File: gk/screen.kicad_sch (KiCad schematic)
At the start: 8 parts, among them J3 Conn_02x27_Top_Bottom, U5 PT4110E89E

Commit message: Update pcb
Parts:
- added C78: 100n, Capacitor_SMD:C_0603_1608Metric, symbol Device:C
- added J9: Conn_01x06, Connector_FFC-FPC:TE_0-1734839-6_1x06-1MP_P0.5mm_Horizontal, symbol Connector_Generic:Conn_01x06
- added R56: 10k, Resistor_SMD:R_0603_1608Metric, symbol Device:R
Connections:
- net GND: now also C78.2, J9.6 (Pin_6), R56.2
- net VCC: now also C78.1, J9.3 (Pin_3)
- new net CTP_INT: J9.5 (Pin_5)
- new net CTP_NRESET: J9.4 (Pin_4), R56.1
- new net I2C4_SCL: J9.1 (Pin_1)
- new net I2C4_SDA: J9.2 (Pin_2)
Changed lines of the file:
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@@
   (junction (at 105.41 54.61) (diameter 0) (color 0 0 0 0)
   )
+  (junction (at 179.07 52.07) (diameter 0) (color 0 0 0 0)
+  )
   (junction (at 140.97 82.55) (diameter 0) (color 0 0 0 0)
   )
@@
   (junction (at 63.5 58.42) (diameter 0) (color 0 0 0 0)
   )
+  (junction (at 209.55 62.23) (diameter 0) (color 0 0 0 0)
+  )
   (junction (at 86.36 48.26) (diameter 0) (color 0 0 0 0)
   )
@@
   (junction (at 88.9 60.96) (diameter 0) (color 0 0 0 0)
   )
+  (junction (at 179.07 62.23) (diameter 0) (color 0 0 0 0)
+  )
   (junction (at 46.99 58.42) (diameter 0) (color 0 0 0 0)
+  )
+  (junction (at 209.55 54.61) (diameter 0) (color 0 0 0 0)
   )
   (no_connect (at 134.62 102.87))
@@
     (stroke (width 0) (type default))
   )
+  (wire (pts (xy 209.55 62.23) (xy 231.14 62.23))
+    (stroke (width 0) (type default))
+  )
   (wire (pts (xy 73.66 69.85) (xy 73.66 67.31))
     (stroke (width 0) (type default))
@@
     (stroke (width 0) (type default))
   )
+  (wire (pts (xy 217.17 54.61) (xy 217.17 57.15))
+    (stroke (width 0) (type default))
+  )
+  (wire (pts (xy 207.01 54.61) (xy 209.55 54.61))
+    (stroke (width 0) (type default))
+  )
   (wire (pts (xy 105.41 48.26) (xy 105.41 54.61))
     (stroke (width 0) (type default))
@@
     (stroke (width 0) (type default))
   )
+  (wire (pts (xy 179.07 62.23) (xy 179.07 59.69))
+    (stroke (width 0) (type default))
+  )
   (wire (pts (xy 82.55 58.42) (xy 86.36 58.42))
     (stroke (width 0) (type default))
@@
     (stroke (width 0) (type default))
   )
+  (wire (pts (xy 179.07 63.5) (xy 179.07 62.23))
+    (stroke (width 0) (type default))
+  )
   (wire (pts (xy 105.41 54.61) (xy 116.84 54.61))
     (stroke (width 0) (type default))
@@
     (stroke (width 0) (type default))
   )
+  (wire (pts (xy 218.44 54.61) (xy 218.44 52.07))
+    (stroke (width 0) (type default))
+  )
   (wire (pts (xy 121.92 49.53) (xy 116.84 49.53))
     (stroke (width 0) (type default))
@@
     (stroke (width 0) (type default))
   )
+  (wire (pts (xy 218.44 52.07) (xy 179.07 52.07))
+    (stroke (width 0) (type default))
+  )
   (wire (pts (xy 60.96 69.85) (xy 73.66 69.85))
     (stroke (width 0) (type default))
@@
     (stroke (width 0) (type default))
   )
+  (wire (pts (xy 231.14 54.61) (xy 218.44 54.61))
+    (stroke (width 0) (type default))
+  )
   (wire (pts (xy 46.99 58.42) (xy 63.5 58.42))
     (stroke (width 0) (type default))
@@
     (stroke (width 0) (type default))
   )
+  (wire (pts (xy 217.17 57.15) (xy 231.14 57.15))
+    (stroke (width 0) (type default))
+  )
   (wire (pts (xy 134.62 115.57) (xy 137.16 115.57))
     (stroke (width 0) (type default))
@@
     (stroke (width 0) (type default))
   )
+  (wire (pts (xy 179.07 62.23) (xy 209.55 62.23))
+    (stroke (width 0) (type default))
+  )
   (wire (pts (xy 63.5 58.42) (xy 64.77 58.42))
     (stroke (width 0) (type default))
   )
+  (wire (pts (xy 209.55 54.61) (xy 217.17 54.61))
+    (stroke (width 0) (type default))
+  )
   (wire (pts (xy 105.41 54.61) (xy 99.06 54.61))
     (stroke (width 0) (type default))
@@
     )
   )
+  (global_label "I2C4_SCL" (shape input) (at 231.14 49.53 180) (fields_autoplaced)
+    (effects (font (size 1.27 1.27)) (justify right))
+    (property "Intersheetrefs" "${INTERSHEET_REFS}" (at 219.4652 49.53 0)
+      (effects (font (size 1.27 1.27)) (justify right) hide)
+    )
+  )
   (global_label "LTDC_R0" (shape input) (at 134.62 49.53 0) (fields_autoplaced)
     (effects (font (size 1.27 1.27)) (justify left))
@@
     )
   )
+  (global_label "CTP_NRESET" (shape input) (at 207.01 54.61 180) (fields_autoplaced)
+    (effects (font (size 1.27 1.27)) (justify right))
+    (property "Intersheetrefs" "${INTERSHEET_REFS}" (at 192.5534 54.61 0)
+      (effects (font (size 1.27 1.27)) (justify right) hide)
+    )
+  )
   (global_label "LTDC_R2" (shape input) (at 134.62 54.61 0) (fields_autoplaced)
     (effects (font (size 1.27 1.27)) (justify left))
@@
     )
   )
+  (global_label "I2C4_SDA" (shape input) (at 231.14 52.07 180) (fields_autoplaced)
+    (effects (font (size 1.27 1.27)) (justify right))
+    (property "Intersheetrefs" "${INTERSHEET_REFS}" (at 219.4047 52.07 0)
+      (effects (font (size 1.27 1.27)) (justify right) hide)
+    )
+  )
+  (global_label "CTP_INT" (shape input) (at 231.14 59.69 180) (fields_autoplaced)
+    (effects (font (size 1.27 1.27)) (justify right))
+    (property "Intersheetrefs" "${INTERSHEET_REFS}" (at 220.8561 59.69 0)
+      (effects (font (size 1.27 1.27)) (justify right) hide)
+    )
+  )
   (global_label "LTDC_G5" (shape input) (at 121.92 110.49 180) (fields_autoplaced)
     (effects (font (size 1.27 1.27)) (justify right))
@@
     (property "Intersheetrefs" "${INTERSHEET_REFS}" (at 111.0314 87.63 0)
       (effects (font (size 1.27 1.27)) (justify right) hide)
+    )
+  )
+  (symbol (lib_id "Device:C") (at 179.07 55.88 0) (unit 1)
+    (in_bom yes) (on_board yes) (dnp no) (fields_autoplaced)
+    (property "Reference" "C78" (at 182.88 55.245 0)
+      (effects (font (size 1.27 1.27)) (justify left))
+    )
+    (property "Value" "100n" (at 182.88 57.785 0)
+      (effects (font (size 1.27 1.27)) (justify left))
+    )
+    (property "Footprint" "Capacitor_SMD:C_0603_1608Metric" (at 180.0352 59.69 0)
+      (effects (font (size 1.27 1.27)) hide)
+    )
+    (property "Datasheet" "~" (at 179.07 55.88 0)
+      (effects (font (size 1.27 1.27)) hide)
+    )
+    (pin "1")
+    (pin "2")
+    (instances
+      (project "gk"
+        (path "/08730ac6-6084-459f-bdf1-86b322355ede/d5be4181-38f9-47fc-b63f-d0d72c8d11e3"
+          (reference "C78") (unit 1)
+        )
+      )
     )
   )
@@
     )
   )
+  (symbol (lib_id "Connector_Generic:Conn_01x06") (at 236.22 54.61 0) (unit 1)
+    (in_bom yes) (on_board yes) (dnp no) (fields_autoplaced)
+    (property "Reference" "J9" (at 238.76 55.245 0)
+      (effects (font (size 1.27 1.27)) (justify left))
+    )
+    (property "Value" "Conn_01x06" (at 238.76 57.785 0)
+      (effects (font (size 1.27 1.27)) (justify left))
+    )
+    (property "Footprint" "Connector_FFC-FPC:TE_0-1734839-6_1x06-1MP_P0.5mm_Horizontal" (at 236.22 54.61 0)
+      (effects (font (size 1.27 1.27)) hide)
+    )
+    (property "Datasheet" "~" (at 236.22 54.61 0)
+      (effects (font (size 1.27 1.27)) hide)
+    )
+    (pin "1")
+    (pin "2")
+    (pin "3")
+    (pin "4")
+    (pin "5")
+    (pin "6")
+    (instances
+      (project "gk"
+        (path "/08730ac6-6084-459f-bdf1-86b322355ede/d5be4181-38f9-47fc-b63f-d0d72c8d11e3"
+          (reference "J9") (unit 1)
+        )
+      )
+    )
+  )
   (symbol (lib_id "power:GND") (at 137.16 116.84 0) (unit 1)
     (in_bom yes) (on_board yes) (dnp no) (fields_autoplaced)
@@
         )
       )
+    )
+  )
+  (symbol (lib_id "Device:R") (at 209.55 58.42 0) (unit 1)
+    (in_bom yes) (on_board yes) (dnp no) (fields_autoplaced)
+    (property "Reference" "R56" (at 212.09 57.785 0)
+      (effects (font (size 1.27 1.27)) (justify left))
+    )
+    (property "Value" "10k" (at 212.09 60.325 0)
+      (effects (font (size 1.27 1.27)) (justify left))
+    )
+    (property "Footprint" "Resistor_SMD:R_0603_1608Metric" (at 207.772 58.42 90)
+      (effects (font (size 1.27 1.27)) hide)
+    )
+    (property "Datasheet" "~" (at 209.55 58.42 0)
+      (effects (font (size 1.27 1.27)) hide)
+    )
+    (pin "1")
+    (pin "2")
+    (instances
+      (project "gk"
+        (path "/08730ac6-6084-459f-bdf1-86b322355ede/d5be4181-38f9-47fc-b63f-d0d72c8d11e3"
+          (reference "R56") (unit 1)
+        )
+      )
+    )
+  )
+  (symbol (lib_id "power:GND") (at 179.07 63.5 0) (unit 1)
+    (in_bom yes) (on_board yes) (dnp no) (fields_autoplaced)
+    (property "Reference" "#PWR068" (at 179.07 69.85 0)
+      (effects (font (size 1.27 1.27)) hide)
+    )
+    (property "Value" "GND" (at 179.07 68.58 0)
+      (effects (font (size 1.27 1.27)))
+    )
+    (property "Footprint" "" (at 179.07 63.5 0)
+      (effects (font (size 1.27 1.27)) hide)
+    )
+    (property "Datasheet" "" (at 179.07 63.5 0)
+      (effects (font (size 1.27 1.27)) hide)
+    )
+    (pin "1")
+    (instances
+      (project "gk"
+        (path "/08730ac6-6084-459f-bdf1-86b322355ede/d5be4181-38f9-47fc-b63f-d0d72c8d11e3"
+          (reference "#PWR068") (unit 1)
+        )
+      )
+    )
+  )
+  (symbol (lib_id "power:VCC") (at 179.07 52.07 0) (unit 1)
+    (in_bom yes) (on_board yes) (dnp no) (fields_autoplaced)
+    (property "Reference" "#PWR067" (at 179.07 55.88 0)
+      (effects (font (size 1.27 1.27)) hide)
+    )
+    (property "Value" "VCC" (at 179.07 48.26 0)
+      (effects (font (size 1.27 1.27)))
+    )
+    (property "Footprint" "" (at 179.07 52.07 0)
+      (effects (font (size 1.27 1.27)) hide)
+    )
+    (property "Datasheet" "" (at 179.07 52.07 0)
+      (effects (font (size 1.27 1.27)) hide)
+    )
+    (pin "1")
+    (instances
+      (project "gk"
+        (path "/08730ac6-6084-459f-bdf1-86b322355ede/d5be4181-38f9-47fc-b63f-d0d72c8d11e3"
+          (reference "#PWR067") (unit 1)
+        )
+      )

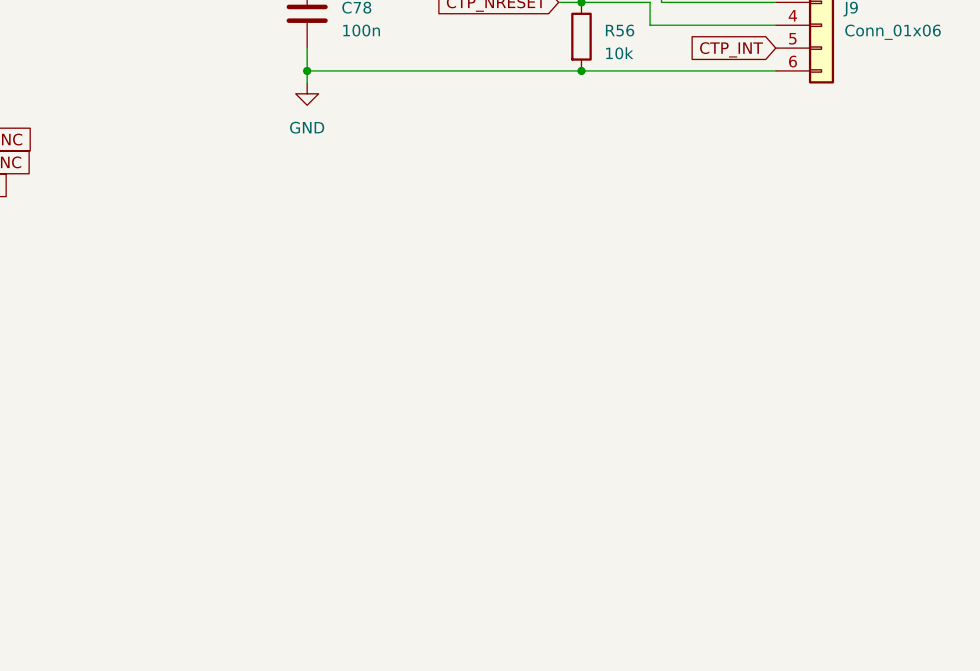
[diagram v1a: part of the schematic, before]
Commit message: Add mount pin for abxy/udlr buttons Fix button spacing Add leds for menu button
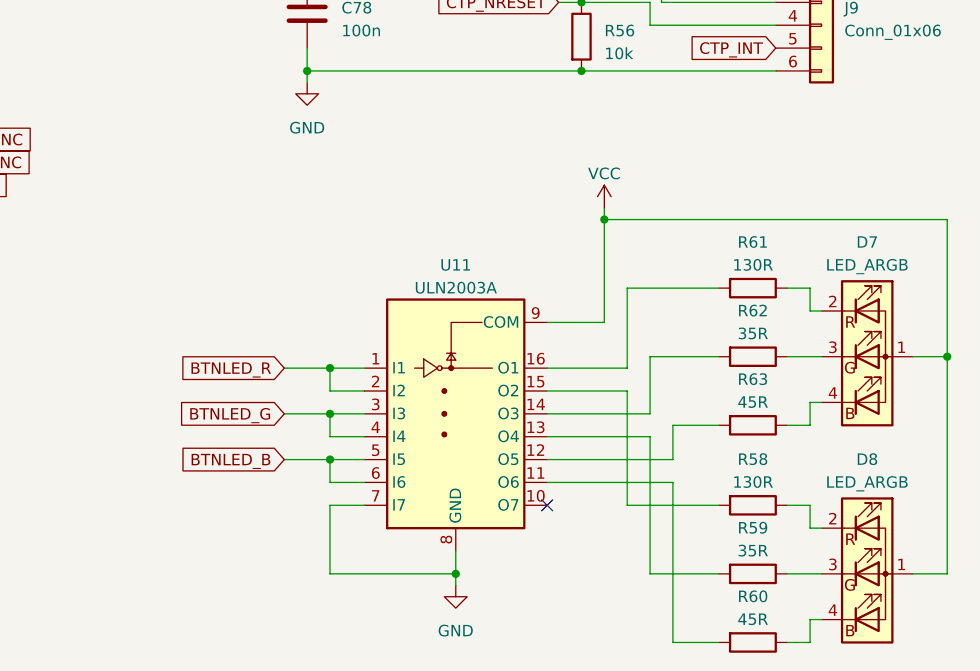
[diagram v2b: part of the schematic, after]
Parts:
- added D7, D8: LED_ARGB, LED_SMD:LED_ASMB-KTF0-0A306, symbol Device:LED_ARGB
- added R58, R61: 130R, Resistor_SMD:R_0603_1608Metric, symbol Device:R
- added R59, R62: 35R, Resistor_SMD:R_0603_1608Metric, symbol Device:R
- added R60, R63: 45R, Resistor_SMD:R_0603_1608Metric, symbol Device:R
- added U11: ULN2003A, Package_SO:SOIC-16W_5.3x10.2mm_P1.27mm, symbol Transistor_Array:ULN2003A
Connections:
- net GND: now also U11.7 (I7), U11.8 (GND)
- net VCC: now also D7.1 (A), D8.1 (A), U11.9 (COM)
- new net: D8.3 (GK), R59.1
- new net: R59.2, U11.13 (O4)
- new net: D7.4 (BK), R63.1
- new net: R63.2, U11.12 (O5)
- new net: D8.2 (RK), R58.1
- new net: D8.4 (BK), R60.1
- new net: R60.2, U11.11 (O6)
- new net: D7.2 (RK), R61.1
- new net: R61.2, U11.16 (O1)
- new net: R62.2, U11.14 (O3)
- new net: R58.2, U11.15 (O2)
- new net: D7.3 (GK), R62.1
- new net BTNLED_B: U11.5 (I5), U11.6 (I6)
- new net BTNLED_G: U11.3 (I3), U11.4 (I4)
- new net BTNLED_R: U11.1 (I1), U11.2 (I2)
- no-connect marks 13 -> 14

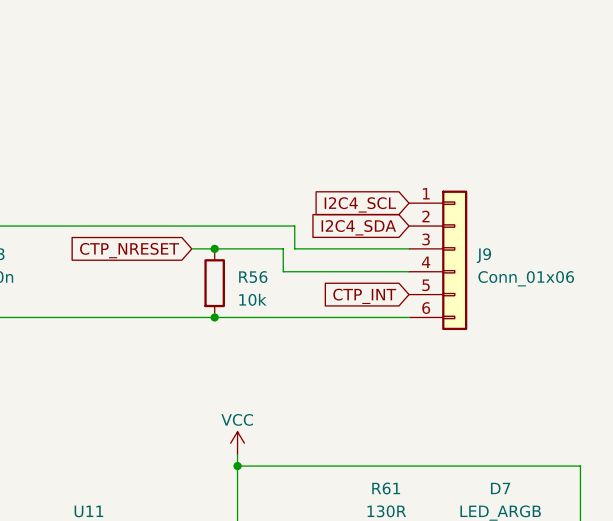
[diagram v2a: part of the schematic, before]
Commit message: Flip lcd sockets to back
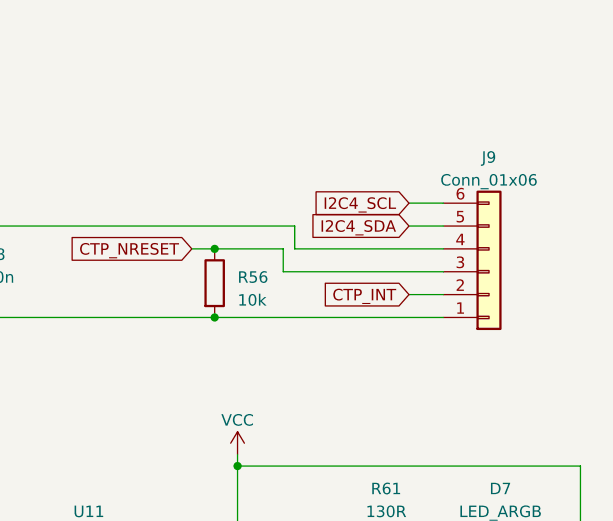
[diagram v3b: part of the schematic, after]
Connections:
- net CTP_INT: now also J9.2 (Pin_2); no longer J9.5 (Pin_5)
- net CTP_NRESET: now also J9.3 (Pin_3); no longer J9.4 (Pin_4)
- net GND: now also J9.1 (Pin_1); no longer J9.6 (Pin_6)
- net I2C4_SCL: now also J9.6 (Pin_6); no longer J9.1 (Pin_1)
- net I2C4_SDA: now also J9.5 (Pin_5); no longer J9.2 (Pin_2)
- net VCC: now also J9.4 (Pin_4); no longer J9.3 (Pin_3)
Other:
- moved on the sheet: J9
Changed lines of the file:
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@@
   (junction (at 105.41 54.61) (diameter 0) (color 0 0 0 0)
   )
+  (junction (at 209.55 62.23) (diameter 0) (color 0 0 0 0)
+  )
   (junction (at 179.07 52.07) (diameter 0) (color 0 0 0 0)
   )
@@
   )
   (junction (at 63.5 58.42) (diameter 0) (color 0 0 0 0)
-  )
-  (junction (at 209.55 62.23) (diameter 0) (color 0 0 0 0)
   )
   (junction (at 250.19 93.98) (diameter 0) (color 0 0 0 0)
@@
     (stroke (width 0) (type default))
   )
+  (wire (pts (xy 209.55 62.23) (xy 234.95 62.23))
+    (stroke (width 0) (type default))
+  )
   (wire (pts (xy 232.41 93.98) (xy 236.22 93.98))
     (stroke (width 0) (type default))
@@
     (stroke (width 0) (type default))
   )
-  (wire (pts (xy 209.55 62.23) (xy 231.14 62.23))
-    (stroke (width 0) (type default))
-  )
   (wire (pts (xy 181.61 110.49) (xy 185.42 110.49))
     (stroke (width 0) (type default))
@@
     (stroke (width 0) (type default))
   )
+  (wire (pts (xy 217.17 57.15) (xy 234.95 57.15))
+    (stroke (width 0) (type default))
+  )
   (wire (pts (xy 232.41 110.49) (xy 234.95 110.49))
     (stroke (width 0) (type default))
@@
     (stroke (width 0) (type default))
   )
+  (wire (pts (xy 231.14 52.07) (xy 234.95 52.07))
+    (stroke (width 0) (type default))
+  )
+  (wire (pts (xy 231.14 59.69) (xy 234.95 59.69))
+    (stroke (width 0) (type default))
+  )
   (wire (pts (xy 224.79 86.36) (xy 214.63 86.36))
     (stroke (width 0) (type default))
@@
     (stroke (width 0) (type default))
   )
-  (wire (pts (xy 231.14 54.61) (xy 218.44 54.61))
-    (stroke (width 0) (type default))
-  )
   (wire (pts (xy 46.99 58.42) (xy 63.5 58.42))
     (stroke (width 0) (type default))
@@
     (stroke (width 0) (type default))
   )
+  (wire (pts (xy 231.14 49.53) (xy 234.95 49.53))
+    (stroke (width 0) (type default))
+  )
   (wire (pts (xy 88.9 60.96) (xy 82.55 60.96))
     (stroke (width 0) (type default))
@@
     (stroke (width 0) (type default))
   )
-  (wire (pts (xy 217.17 57.15) (xy 231.14 57.15))
+  (wire (pts (xy 218.44 54.61) (xy 234.95 54.61))
     (stroke (width 0) (type default))
   )
@@
     )
   )
-  (symbol (lib_id "Connector_Generic:Conn_01x06") (at 236.22 54.61 0) (unit 1)
-    (in_bom yes) (on_board yes) (dnp no) (fields_autoplaced)
-    (property "Reference" "J9" (at 238.76 55.245 0)
-      (effects (font (size 1.27 1.27)) (justify left))
-    )
-    (property "Value" "Conn_01x06" (at 238.76 57.785 0)
-      (effects (font (size 1.27 1.27)) (justify left))
-    )
-    (property "Footprint" "Connector_FFC-FPC:TE_0-1734839-6_1x06-1MP_P0.5mm_Horizontal" (at 236.22 54.61 0)
-      (effects (font (size 1.27 1.27)) hide)
-    )
-    (property "Datasheet" "~" (at 236.22 54.61 0)
-      (effects (font (size 1.27 1.27)) hide)
-    )
+  (symbol (lib_id "Connector_Generic:Conn_01x06") (at 240.03 57.15 0) (mirror x) (unit 1)
+    (in_bom yes) (on_board yes) (dnp no)
+    (property "Reference" "J9" (at 240.03 44.45 0)
+      (effects (font (size 1.27 1.27)))
+    )
+    (property "Value" "Conn_01x06" (at 240.03 46.99 0)
+      (effects (font (size 1.27 1.27)))
+    )
+    (property "Footprint" "Connector_FFC-FPC:TE_0-1734839-6_1x06-1MP_P0.5mm_Horizontal" (at 240.03 57.15 0)
+      (effects (font (size 1.27 1.27)) hide)
+    )
+    (property "Datasheet" "~" (at 240.03 57.15 0)
+      (effects (font (size 1.27 1.27)) hide)
+    )
